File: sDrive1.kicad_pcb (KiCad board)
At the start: 2 copper layers, 50 x 37 mm, 35 parts, among them U1 DRV8323SRTAT, U3 24LC01

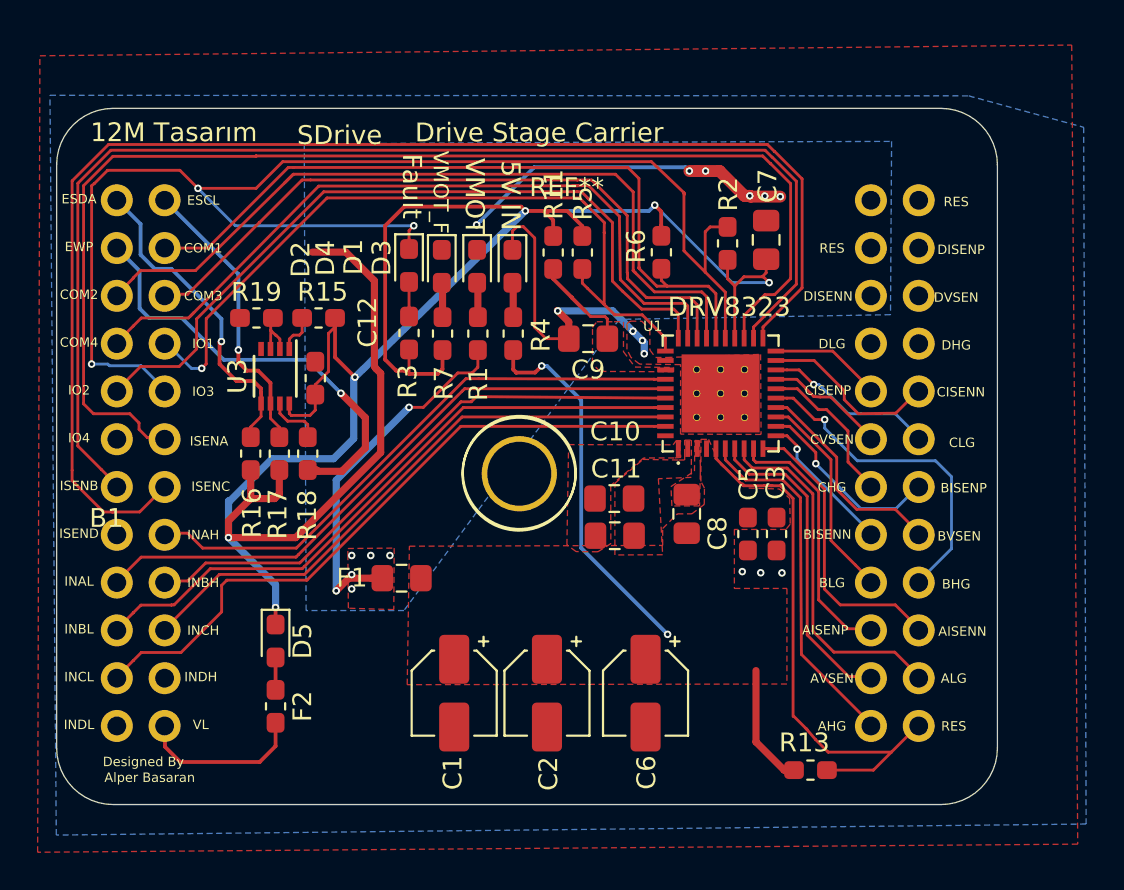
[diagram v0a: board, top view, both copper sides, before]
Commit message: add voltage supply sense resistors
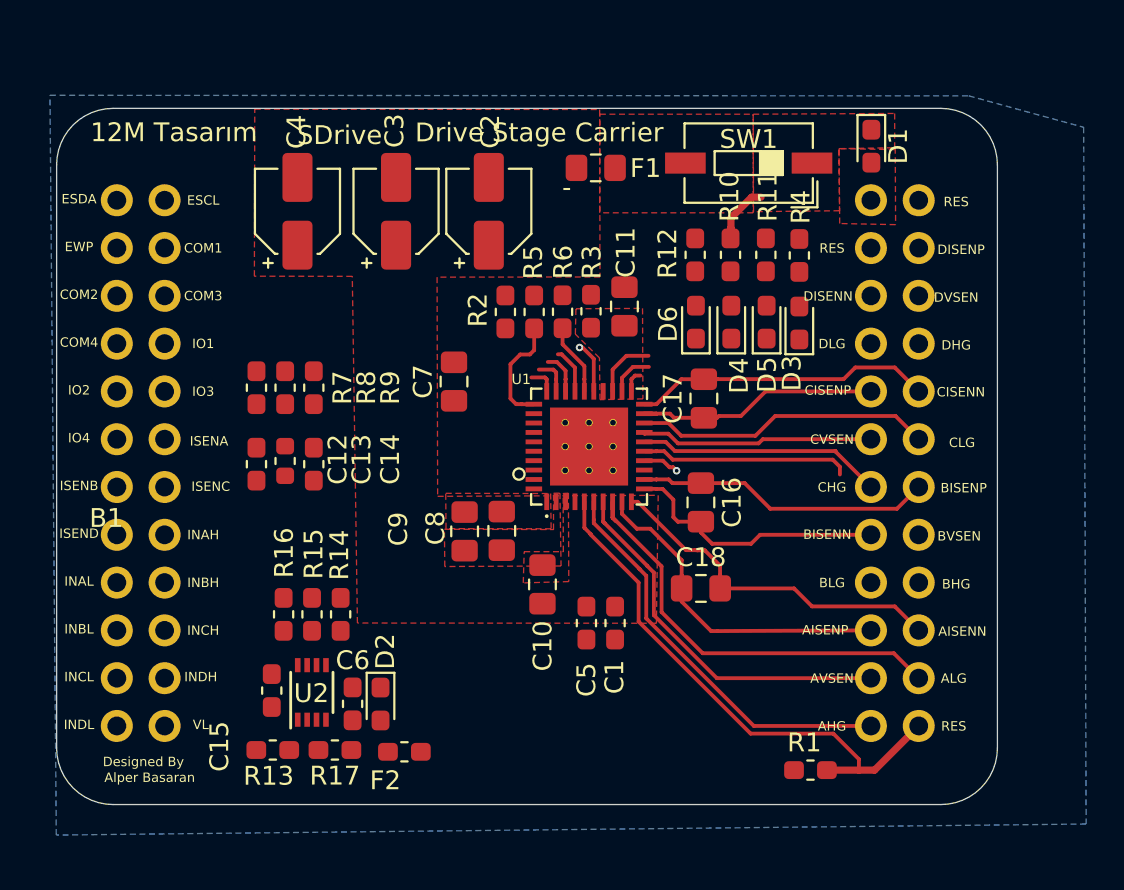
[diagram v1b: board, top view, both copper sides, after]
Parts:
- removed the C3 at (37.8, -14.1)
- removed the R1 at (21.9, -24.7)
- added C1: X7R, 47-nF, Capacitor_SMD:C_0603_1608Metric_Pad1.05x0.95mm_HandSolder, F.Cu at (29.2, -9.34)
- added C12: X7R, 2200pF, Capacitor_SMD:C_0603_1608Metric_Pad1.05x0.95mm_HandSolder, F.Cu at (10.2, -17.8)
- added C13: X7R, 2200pF, Capacitor_SMD:C_0603_1608Metric, F.Cu at (11.7, -17.9)
- added C14: X7R, 0.1µF, Capacitor_SMD:C_0603_1608Metric_Pad1.05x0.95mm_HandSolder, F.Cu at (13.2, -17.8)
- added C16: 1000pF, Capacitor_SMD:C_0805_2012Metric_Pad1.15x1.40mm_HandSolder, F.Cu at (33.8, -15.7)
- added C17: 1000pF, Capacitor_SMD:C_0805_2012Metric_Pad1.15x1.40mm_HandSolder, F.Cu at (33.9, -21.3)
- added C18: 1000pF, Capacitor_SMD:C_0805_2012Metric_Pad1.15x1.40mm_HandSolder, F.Cu at (33.8, -11.2)
- added C6: X7R, 47-nF, Capacitor_SMD:C_0603_1608Metric_Pad1.05x0.95mm_HandSolder, F.Cu at (15.3, -5.04)
- added D6: YELLOW, LED_SMD:LED_0603_1608Metric_Pad1.05x0.95mm_HandSolder, F.Cu at (33.5, -25.3)
- added R10: 0603 1k, Resistor_SMD:R_0603_1608Metric_Pad1.05x0.95mm_HandSolder, F.Cu at (35.4, -28.9)
- added R12: 0603 2k, Resistor_SMD:R_0603_1608Metric_Pad1.05x0.95mm_HandSolder, F.Cu at (33.5, -28.9)
- added R8: 0603 1k, Resistor_SMD:R_0603_1608Metric_Pad1.05x0.95mm_HandSolder, F.Cu at (11.7, -21.8)
- added R9: 0603 1k, Resistor_SMD:R_0603_1608Metric_Pad1.05x0.95mm_HandSolder, F.Cu at (10.2, -21.8)
- added SW1: SW_Push_Open, Button_Switch_SMD:SW_DIP_SPSTx01_Slide_6.7x4.1mm_W6.73mm_P2.54mm_LowProfile_JPin, F.Cu at (36.3, -33.8)
- C10: value X7R, 47-nF -> X7R, 1µF
- C11: value X7R, 47-nF -> X7R, 0.1µF
- C7: value X7R, 0.1µF -> X7R, 1µF
- C8, C9: value X7R, 1µF -> X7R, 47-nF
- D1: value YELLOW -> D_Schottky; footprint LED_SMD:LED_0603_1608Metric_Pad1.05x0.95mm_HandSolder -> Diode_SMD:D_0603_1608Metric_Pad1.05x0.95mm_HandSolder
- D2: value RED -> D_Schottky; footprint LED_SMD:LED_0603_1608Metric_Pad1.05x0.95mm_HandSolder -> Diode_SMD:D_0603_1608Metric_Pad1.05x0.95mm_HandSolder
- D3: value YELLOW -> RED
- D5: value D_Schottky -> YELLOW; footprint Diode_SMD:D_0603_1608Metric_Pad1.05x0.95mm_HandSolder -> LED_SMD:LED_0603_1608Metric_Pad1.05x0.95mm_HandSolder
- R11: value R -> 0603 1k
- R4: value 0603 2k -> R
- moved C4 31.6 mm to (12.3, -31.2), turned to 90 degrees
- moved D5 31.1 mm to (37.3, -25.3), turned to 90 degrees
- moved C3 26.8 mm to (17.6, -31.2), turned to 90 degrees
- moved C2 25.7 mm to (22.5, -31.2), turned to 90 degrees
- moved F1 24.1 mm to (28.2, -33.5), turned to 0 degrees
- moved D2 23.4 mm to (16.8, -5.03)
- moved R17 23.3 mm to (14.3, -2.59), turned to 0 degrees
- moved R13 23.1 mm to (11.0, -2.59), turned to 0 degrees
- moved D1 21.9 mm to (42.8, -34.7)
- moved C7 18.2 mm to (20.7, -22.2)
- moved U2 16.9 mm to (13.1, -5.65), turned to 90 degrees
- moved C15 16.8 mm to (11.0, -5.75), turned to 270 degrees
- moved R4 15.8 mm to (39.0, -28.9), turned to 270 degrees
- moved D4 15.7 mm to (35.4, -25.3), turned to 90 degrees
- moved D3 15.5 mm to (39.0, -25.3), turned to 90 degrees
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- renumbered C12 to C15, C1 to C2, C2 to C3, C6 to C4, R13 to R1, R15 to R13, R16 to R14, R17 to R15, R18 to R16, R19 to R17, U3 to U2
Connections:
- net Net-(B1-Pad15) renamed /Drive_Stage/ISEN_D
- B1 pad 12: /Drive_Stage/SOA -> /Drive_Stage/ISEN_A
- B1 pad 13: /Drive_Stage/SOB -> /Drive_Stage/ISEN_B
- B1 pad 14: /Drive_Stage/SOC -> /Drive_Stage/ISEN_C
- B1 pad 33: /Drive_Stage/SNC -> /Drive_Stage/SPC
- B1 pad 34: /Drive_Stage/SPC -> /Drive_Stage/SNC
- C10 pad 1: /Drive_Stage/CPH -> /Drive_Stage/VM_Protected
- C10 pad 2: /Drive_Stage/CPL -> /Drive_Stage/VCP
- C11 pad 1: /Drive_Stage/CPH -> /Drive_Stage/5V
- C11 pad 2: /Drive_Stage/CPL -> GND
- C7 pad 1: /Drive_Stage/5V -> /Drive_Stage/DVDD
- C8 pad 1: /Drive_Stage/VM_Protected -> /Drive_Stage/CPH
- C8 pad 2: /Drive_Stage/VCP -> /Drive_Stage/CPL
- C9 pad 1: /Drive_Stage/DVDD -> /Drive_Stage/CPH
- C9 pad 2: GND -> /Drive_Stage/CPL
- D1 pad 1: GND -> /Drive_Stage/VM
- D1 pad 2: Net-(D1-Pad2) -> VCC
- D2 pad 1: /Drive_Stage/nFAULT -> /Drive_Stage/5V
- D3 pad 1: GND -> /Drive_Stage/nFAULT
- D5 pad 1: /Drive_Stage/5V -> GND
- F1 pad 2: VCC -> Net-(F1-Pad2)
- F2 pad 1: Net-(D5-Pad2) -> Net-(D2-Pad2)
- R11 pad 2: /Drive_Stage/DVDD -> Net-(D5-Pad2)
- R2 pad 2: /Drive_Stage/nFAULT -> /Drive_Stage/DVDD
- R3 pad 2: Net-(D2-Pad2) -> /Drive_Stage/nFAULT
- R4 pad 1: /Drive_Stage/VM_Protected -> /Drive_Stage/5V
- R7 pad 1: /Drive_Stage/5V -> /Drive_Stage/ISEN_A
- R7 pad 2: Net-(D4-Pad2) -> /Drive_Stage/SOA
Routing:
- net /Drive_Stage/5V: track 124.0 -> 0.00 mm, vias 6 -> 0
- net /Drive_Stage/SOC: track 71.8 -> 1.21 mm
- net /Drive_Stage/nFAULT: track 73.2 -> 2.74 mm, vias 3 -> 1
- net /Drive_Stage/SOB: track 65.8 -> 2.39 mm
- net /Drive_Stage/SOA: track 65.3 -> 3.37 mm
- net /Drive_Stage/SDI: track 42.1 -> 2.46 mm
- net /Drive_Stage/ENABLE: track 40.9 -> 1.50 mm
- net /Drive_Stage/NSCS: track 40.6 -> 1.99 mm
- net /Drive_Stage/SDO: track 40.1 -> 3.84 mm
- net /Drive_Stage/CAL: track 41.6 -> 5.91 mm, vias 1 -> 0
- net /Drive_Stage/INLC: track 35.5 -> 0.00 mm
- net /Drive_Stage/SCLK: track 37.3 -> 2.24 mm
- net GND: track 35.0 -> 0.00 mm, vias 13 -> 0
- net /Drive_Stage/INLB: track 34.6 -> 0.00 mm
- net /Drive_Stage/INLA: track 33.4 -> 0.00 mm
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- added copper zone on F.Cu, net /Drive_Stage/5V
- added copper zone on F.Cu, net /Drive_Stage/VM
- added copper zone on F.Cu, net Net-(F1-Pad2)
- removed copper zone on F.Cu, net /Drive_Stage/DVDD
- removed copper zone on F.Cu, net GND
- removed copper zone on B.Cu, net VCC
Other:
- net class Default: clearance 0.1524 -> 0.2032
- rule trace_clearance: 0.1524 -> 0.2032
- board text removed: "5V IN"
- board text removed: "DRV8323"
- board text removed: "Fault"
- board text removed: "VMOT"
- board text removed: "VMOT_F"

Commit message: update production files
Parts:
- added R18: R, Resistor_SMD:R_0603_1608Metric_Pad1.05x0.95mm_HandSolder, F.Cu at (20.5, -7.72)
- added R19: R, Resistor_SMD:R_0603_1608Metric_Pad1.05x0.95mm_HandSolder, F.Cu at (20.5, -6.21)
- C16, C17, C18: footprint Capacitor_SMD:C_0805_2012Metric_Pad1.15x1.40mm_HandSolder -> Capacitor_SMD:C_0603_1608Metric_Pad1.05x0.95mm_HandSolder
- moved C6 10.6 mm to (5.55, -0.90), turned to 180 degrees
- moved F2 8.75 mm to (9.38, -3.85), turned to 180 degrees
- moved D2 7.84 mm to (9.39, -2.35), turned to 0 degrees
- moved R13 2.36 mm to (9.40, -0.88)
- moved C14 1.40 mm to (14.6, -17.8)
- moved R7 1.40 mm to (14.6, -21.8)
- moved C16 1.25 mm to (34.9, -15.2)
- moved R16 0.90 mm to (11.6, -10.7)
- moved R14 0.90 mm to (14.6, -10.7)
- moved R15 0.90 mm to (13.1, -10.7)
- moved R8 0.72 mm to (12.4, -21.8)
- moved C13 0.72 mm to (12.4, -17.9)
- moved C15 0.72 mm to (10.8, -6.45)
- moved C17 0.63 mm to (34.5, -21.4)
- moved R17 0.50 mm to (14.6, -2.19)
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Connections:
- B1 pad 23: Net-(B1-Pad23) -> /Drive_Stage/VM_VSEN
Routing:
- net /Drive_Stage/5V: track 0.00 -> 99.8 mm, vias 0 -> 4
- net /Drive_Stage/EEPROM_SCL: track 0.00 -> 53.3 mm, vias 0 -> 1
- net /Drive_Stage/nFAULT: track 2.74 -> 54.9 mm, vias 1 -> 4
- net /Drive_Stage/EEPROM_SDA: track 0.00 -> 50.0 mm, vias 0 -> 1
- net /Drive_Stage/EEPROM_WP: track 0.00 -> 38.5 mm, vias 0 -> 1
- net /Drive_Stage/SDO: track 3.84 -> 42.2 mm, vias 0 -> 1
- net /Drive_Stage/ENABLE: track 1.50 -> 34.6 mm, vias 0 -> 1
- net /Drive_Stage/SDI: track 2.46 -> 33.9 mm, vias 0 -> 1
- net /Drive_Stage/SCLK: track 2.24 -> 33.0 mm, vias 0 -> 1
- net /Drive_Stage/VM_VSEN: track 0.00 -> 28.9 mm
- net /Drive_Stage/NSCS: track 1.99 -> 30.8 mm, vias 0 -> 1
- net /Drive_Stage/VM_Protected: track 0.00 -> 27.4 mm
- net /Drive_Stage/INLC: track 0.00 -> 26.6 mm, vias 0 -> 1
- net /Drive_Stage/INLB: track 0.00 -> 26.2 mm, vias 0 -> 1
- net /Drive_Stage/INLA: track 0.00 -> 25.4 mm, vias 0 -> 1
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- added copper zone on F.Cu, net /Drive_Stage/DVDD
- added copper zone on F.Cu, net GND
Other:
- net class Default: clearance 0.2032 -> 0.1524
- rule trace_clearance: 0.2032 -> 0.1524
- board text added: "DRV8323 Carrier"

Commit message: move VMsen to pin 8
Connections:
- B1 pad 11: Net-(B1-Pad11) -> /Drive_Stage/VM_VSEN
- B1 pad 23: /Drive_Stage/VM_VSEN -> Net-(B1-Pad23)
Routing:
- net /Drive_Stage/VM_VSEN: track 28.9 -> 30.4 mm
